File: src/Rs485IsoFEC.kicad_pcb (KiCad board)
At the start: 2 copper layers, 24 x 27.9 mm, 28 parts, among them J1 B4B-XH-A, P1 105444-0001, Q1 DMP3099L-13, U1 FT232RL, U2 ADM2682E

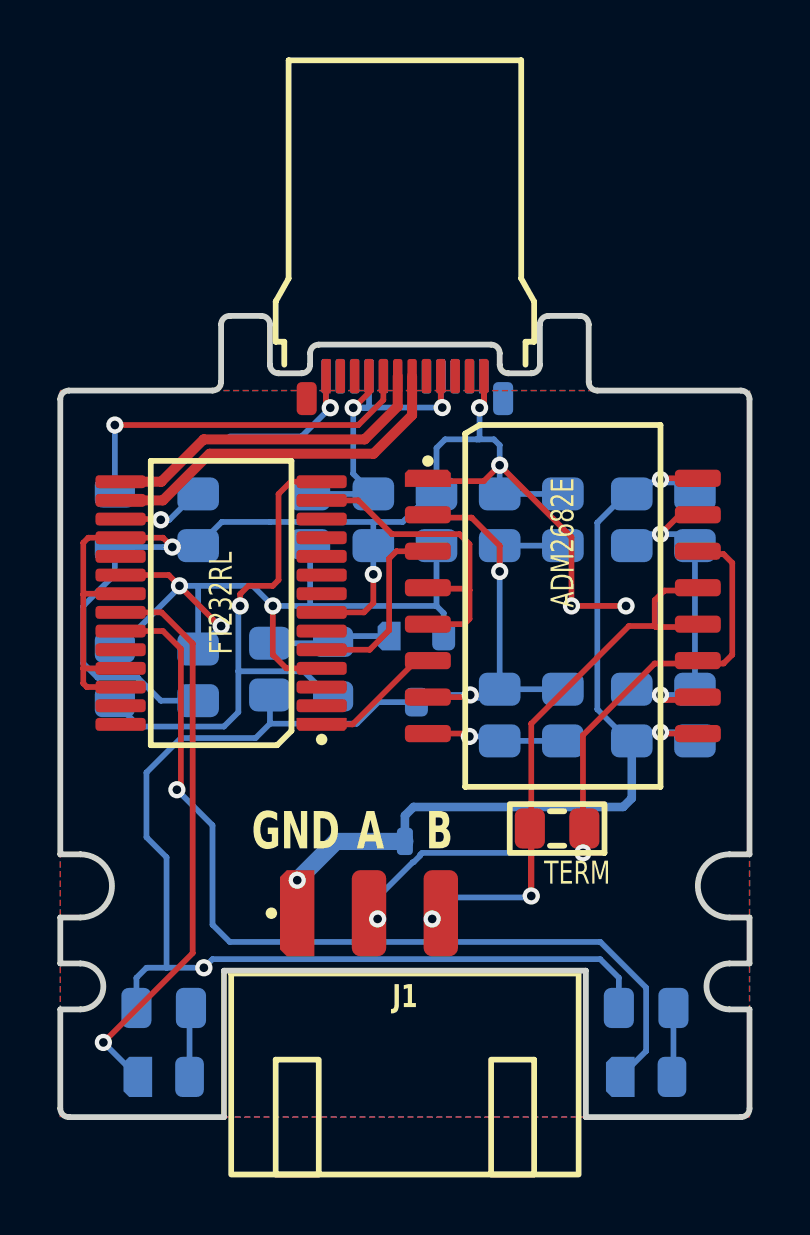
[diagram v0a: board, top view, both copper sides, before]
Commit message: Updated connector to solder all 4 pins
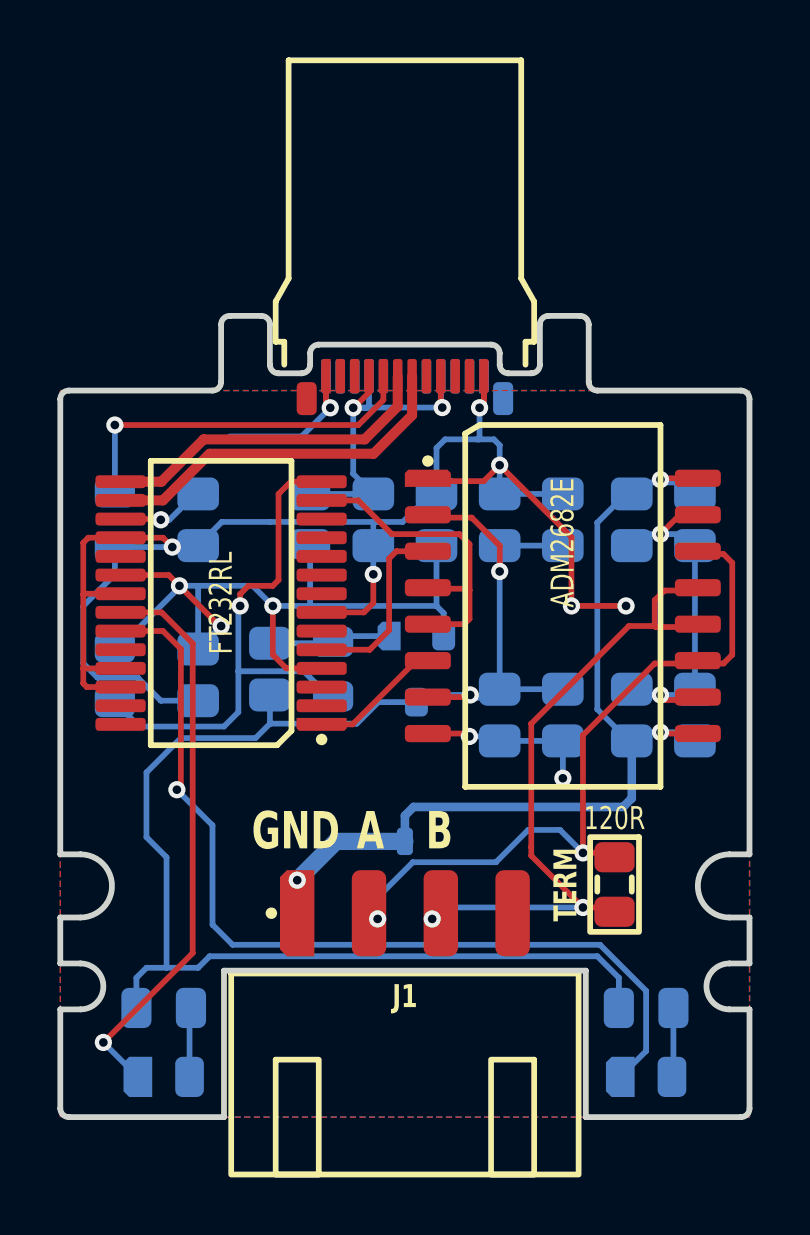
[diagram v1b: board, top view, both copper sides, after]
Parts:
- R1: value TERM -> 120R
- moved R1 2.79 mm to (39.3, 39.8), turned to -90 degrees
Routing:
- net ISO_B: track 23.0 -> 24.7 mm
- net GND: track 72.4 -> 73.7 mm, vias 8 -> 9
- net ISO_A: track 24.3 -> 25.1 mm
- net 5V_SW: track 56.4 -> 56.3 mm, vias 3 -> 2
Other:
- board text added: "TERM"
